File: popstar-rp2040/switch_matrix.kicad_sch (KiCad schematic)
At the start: 0 parts

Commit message: Added surface-mounted LEDs for shinethrough on WKL blockers.
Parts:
- added C18, C19, C20, C21, C22, C23, C24: 100nF, symbol Device:C_Small
- added D1, D10, D11, D12, D2, D3, D4, D5, D6, D7, D8, D9: WS2812_2020, marbastlib-various:LED_WS2812_2020, symbol marbastlib-various:WS2812_2020
- added U5: 74AHCT1G125, Package_TO_SOT_SMD:SOT-23-5, symbol 74xGxx:74AHCT1G125
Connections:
- new net: D2.1 (DOUT), D3.3 (DIN)
- new net: D1.1 (DOUT), D2.3 (DIN)
- new net: D5.1 (DOUT), D6.3 (DIN)
- new net: D4.1 (DOUT), D5.3 (DIN)
- new net: D11.1 (DOUT), D12.3 (DIN)
- new net: D10.1 (DOUT), D11.3 (DIN)
- new net: D3.1 (DOUT), D4.3 (DIN)
- new net: D6.1 (DOUT), D7.3 (DIN)
- new net: D10.3 (DIN), D9.1 (DOUT)
- new net: D8.1 (DOUT), D9.3 (DIN)
- new net: D7.1 (DOUT), D8.3 (DIN)
- new net +5V: C18.1, C19.1, C20.1, C21.1, C22.1, C23.1, C24.1, D1.4 (VDD), D10.4 (VDD), D11.4 (VDD), D12.4 (VDD), D2.4 (VDD), D3.4 (VDD), D4.4 (VDD), D5.4 (VDD), D6.4 (VDD), D7.4 (VDD), D8.4 (VDD), D9.4 (VDD), U5.5 (VCC)
- new net ARGB_3V3: U5.2
- new net ARGB_5V: D1.3 (DIN), U5.4
- new net GND: C18.2, C19.2, C20.2, C21.2, C22.2, C23.2, C24.2, D1.2 (VSS), D10.2 (VSS), D11.2 (VSS), D12.2 (VSS), D2.2 (VSS), D3.2 (VSS), D4.2 (VSS), D5.2 (VSS), D6.2 (VSS), D7.2 (VSS), D8.2 (VSS), D9.2 (VSS), U5.1, U5.3 (GND)
- no-connect marks 0 -> 1

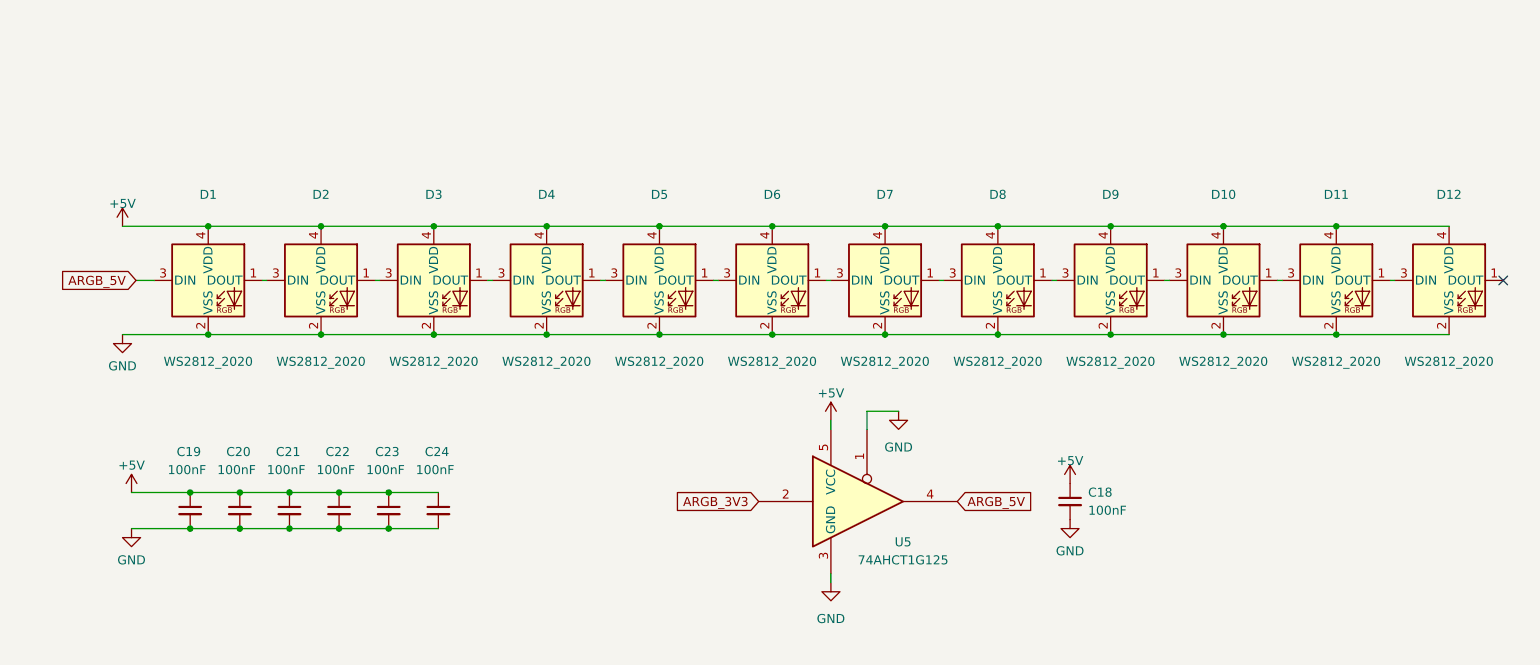
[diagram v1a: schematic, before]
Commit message: Cleaned up LED schematic impl.
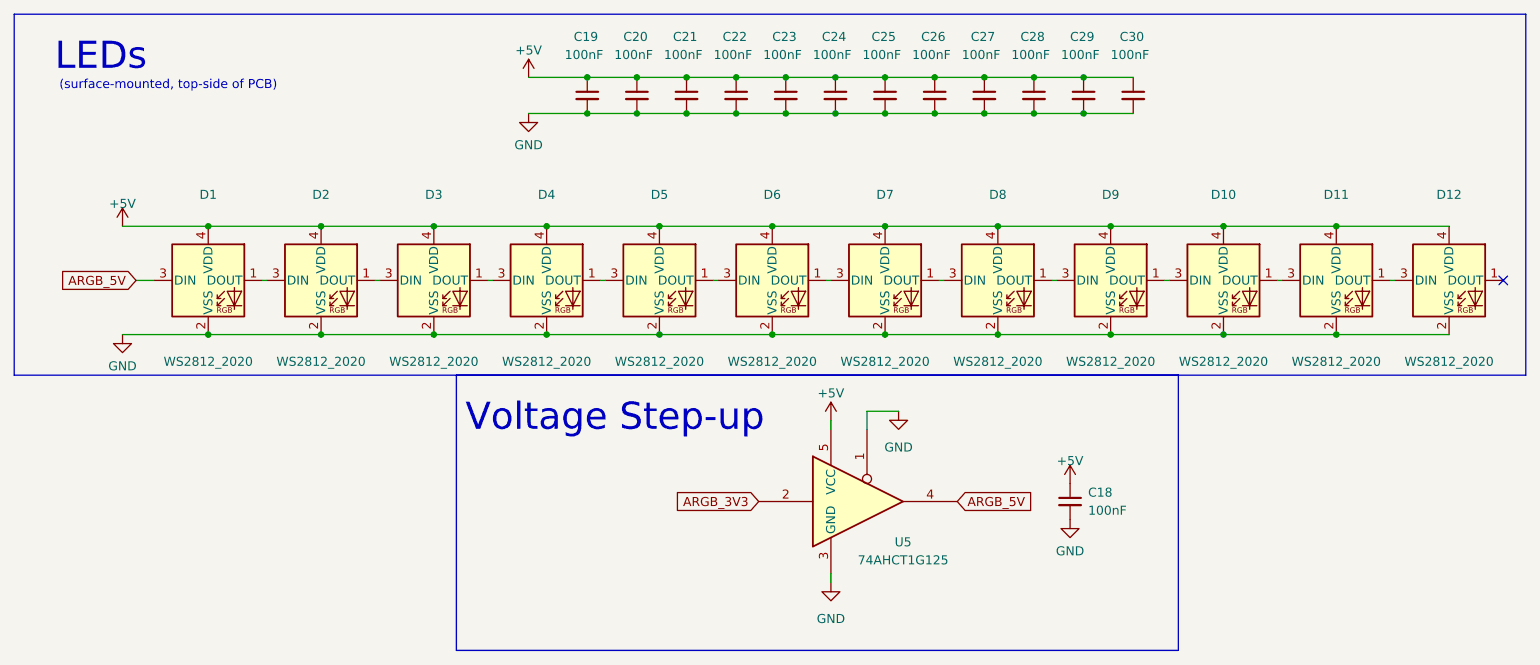
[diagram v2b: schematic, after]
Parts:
- added C25, C26, C27, C28, C29, C30: 100nF, symbol Device:C_Small
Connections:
- net +5V: now also C25.1, C26.1, C27.1, C28.1, C29.1, C30.1
- net GND: now also C25.2, C26.2, C27.2, C28.2, C29.2, C30.2
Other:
- note added: "(surface-mounted, top-side of PCB)"
- note added: "LEDs"
- note added: "Voltage Step-up"
- moved on the sheet: C19, C20, C21, C22, C23, C24

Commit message: Added BOM spreadsheet, updated components with LCSC part numbers and footprints.
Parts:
- C18, C19, C20, C21, C22, C23, C24, C25, C26, C27, C28, C29, C30: footprint (none) -> Capacitor_SMD:C_0402_1005Metric; LCSC (none) -> C1525
- U5: LCSC (none) -> C7484
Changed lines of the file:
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@@
       (effects (font (size 1.27 1.27)) (justify left))
     )
-    (property "Footprint" "" (at 170.18 119.38 0)
+    (property "Footprint" "Capacitor_SMD:C_0402_1005Metric" (at 170.18 119.38 0)
       (effects (font (size 1.27 1.27)) hide)
     )
@@
       (effects (font (size 1.27 1.27)) hide)
     )
+    (property "LCSC" "C1525" (at 170.18 119.38 0)
+      (effects (font (size 1.27 1.27)) hide)
+    )
     (pin "1")
     (pin "2")
@@
       (effects (font (size 1.27 1.27)) (justify left))
     )
-    (property "Footprint" "" (at 163.195 119.38 0)
+    (property "Footprint" "Capacitor_SMD:C_0402_1005Metric" (at 163.195 119.38 0)
       (effects (font (size 1.27 1.27)) hide)
     )
     (property "Datasheet" "~" (at 163.195 119.38 0)
+      (effects (font (size 1.27 1.27)) hide)
+    )
+    (property "LCSC" "C1525" (at 163.195 119.38 0)
       (effects (font (size 1.27 1.27)) hide)
     )
@@
       (effects (font (size 1.27 1.27)) (justify left))
     )
-    (property "Footprint" "" (at 93.345 119.38 0)
+    (property "Footprint" "Capacitor_SMD:C_0402_1005Metric" (at 93.345 119.38 0)
       (effects (font (size 1.27 1.27)) hide)
     )
@@
       (effects (font (size 1.27 1.27)) hide)
     )
+    (property "LCSC" "C1525" (at 93.345 119.38 0)
+      (effects (font (size 1.27 1.27)) hide)
+    )
     (pin "1")
     (pin "2")
@@
       (effects (font (size 1.27 1.27)) (justify left))
     )
-    (property "Footprint" "" (at 121.285 119.38 0)
+    (property "Footprint" "Capacitor_SMD:C_0402_1005Metric" (at 121.285 119.38 0)
       (effects (font (size 1.27 1.27)) hide)
     )
@@
       (effects (font (size 1.27 1.27)) hide)
     )
+    (property "LCSC" "C1525" (at 121.285 119.38 0)
+      (effects (font (size 1.27 1.27)) hide)
+    )
     (pin "1")
     (pin "2")
@@
       (effects (font (size 1.27 1.27)) (justify left))
     )
-    (property "Footprint" "" (at 128.27 119.38 0)
+    (property "Footprint" "Capacitor_SMD:C_0402_1005Metric" (at 128.27 119.38 0)
       (effects (font (size 1.27 1.27)) hide)
     )
@@
       (effects (font (size 1.27 1.27)) hide)
     )
+    (property "LCSC" "C1525" (at 128.27 119.38 0)
+      (effects (font (size 1.27 1.27)) hide)
+    )
     (pin "1")
     (pin "2")
@@
       (effects (font (size 1.27 1.27)) (justify left))
     )
-    (property "Footprint" "" (at 161.29 176.53 0)
+    (property "Footprint" "Capacitor_SMD:C_0402_1005Metric" (at 161.29 176.53 0)
       (effects (font (size 1.27 1.27)) hide)
     )
     (property "Datasheet" "~" (at 161.29 176.53 0)
+      (effects (font (size 1.27 1.27)) hide)
+    )
+    (property "LCSC" "C1525" (at 161.29 176.53 0)
       (effects (font (size 1.27 1.27)) hide)
     )
@@
       (effects (font (size 1.27 1.27)) (justify left))
     )
-    (property "Footprint" "" (at 142.24 119.38 0)
+    (property "Footprint" "Capacitor_SMD:C_0402_1005Metric" (at 142.24 119.38 0)
       (effects (font (size 1.27 1.27)) hide)
     )
@@
       (effects (font (size 1.27 1.27)) hide)
     )
+    (property "LCSC" "C1525" (at 142.24 119.38 0)
+      (effects (font (size 1.27 1.27)) hide)
+    )
     (pin "1")
     (pin "2")
@@
       (effects (font (size 1.27 1.27)) (justify left))
     )
-    (property "Footprint" "" (at 107.315 119.38 0)
+    (property "Footprint" "Capacitor_SMD:C_0402_1005Metric" (at 107.315 119.38 0)
       (effects (font (size 1.27 1.27)) hide)
     )
     (property "Datasheet" "~" (at 107.315 119.38 0)
+      (effects (font (size 1.27 1.27)) hide)
+    )
+    (property "LCSC" "C1525" (at 107.315 119.38 0)
       (effects (font (size 1.27 1.27)) hide)
     )
@@
       (effects (font (size 1.27 1.27)) (justify left))
     )
-    (property "Footprint" "" (at 100.33 119.38 0)
+    (property "Footprint" "Capacitor_SMD:C_0402_1005Metric" (at 100.33 119.38 0)
       (effects (font (size 1.27 1.27)) hide)
     )
@@
       (effects (font (size 1.27 1.27)) hide)
     )
+    (property "LCSC" "C1525" (at 100.33 119.38 0)
+      (effects (font (size 1.27 1.27)) hide)
+    )
     (pin "1")
     (pin "2")
@@
       (effects (font (size 1.27 1.27)) hide)
     )
+    (property "LCSC" "C7484" (at 132.715 176.53 0)
+      (effects (font (size 1.27 1.27)) hide)
+    )
     (pin "1")
     (pin "2")
@@
       (effects (font (size 1.27 1.27)) (justify left))
     )
-    (property "Footprint" "" (at 156.21 119.38 0)
+    (property "Footprint" "Capacitor_SMD:C_0402_1005Metric" (at 156.21 119.38 0)
       (effects (font (size 1.27 1.27)) hide)
     )
     (property "Datasheet" "~" (at 156.21 119.38 0)
+      (effects (font (size 1.27 1.27)) hide)
+    )
+    (property "LCSC" "C1525" (at 156.21 119.38 0)
       (effects (font (size 1.27 1.27)) hide)
     )
@@
       (effects (font (size 1.27 1.27)) (justify left))
     )
-    (property "Footprint" "" (at 114.3 119.38 0)
+    (property "Footprint" "Capacitor_SMD:C_0402_1005Metric" (at 114.3 119.38 0)
       (effects (font (size 1.27 1.27)) hide)
     )
@@
       (effects (font (size 1.27 1.27)) hide)
     )
+    (property "LCSC" "C1525" (at 114.3 119.38 0)
+      (effects (font (size 1.27 1.27)) hide)
+    )
     (pin "1")
     (pin "2")
@@
       (effects (font (size 1.27 1.27)) (justify left))
     )
-    (property "Footprint" "" (at 149.225 119.38 0)
+    (property "Footprint" "Capacitor_SMD:C_0402_1005Metric" (at 149.225 119.38 0)
       (effects (font (size 1.27 1.27)) hide)
     )
@@
       (effects (font (size 1.27 1.27)) hide)
     )
+    (property "LCSC" "C1525" (at 149.225 119.38 0)
+      (effects (font (size 1.27 1.27)) hide)
+    )
     (pin "1")
     (pin "2")
@@
       (effects (font (size 1.27 1.27)) (justify left))
     )
-    (property "Footprint" "" (at 135.255 119.38 0)
+    (property "Footprint" "Capacitor_SMD:C_0402_1005Metric" (at 135.255 119.38 0)
       (effects (font (size 1.27 1.27)) hide)
     )
@@
       (effects (font (size 1.27 1.27)) hide)
     )
+    (property "LCSC" "C1525" (at 135.255 119.38 0)
+      (effects (font (size 1.27 1.27)) hide)
+    )

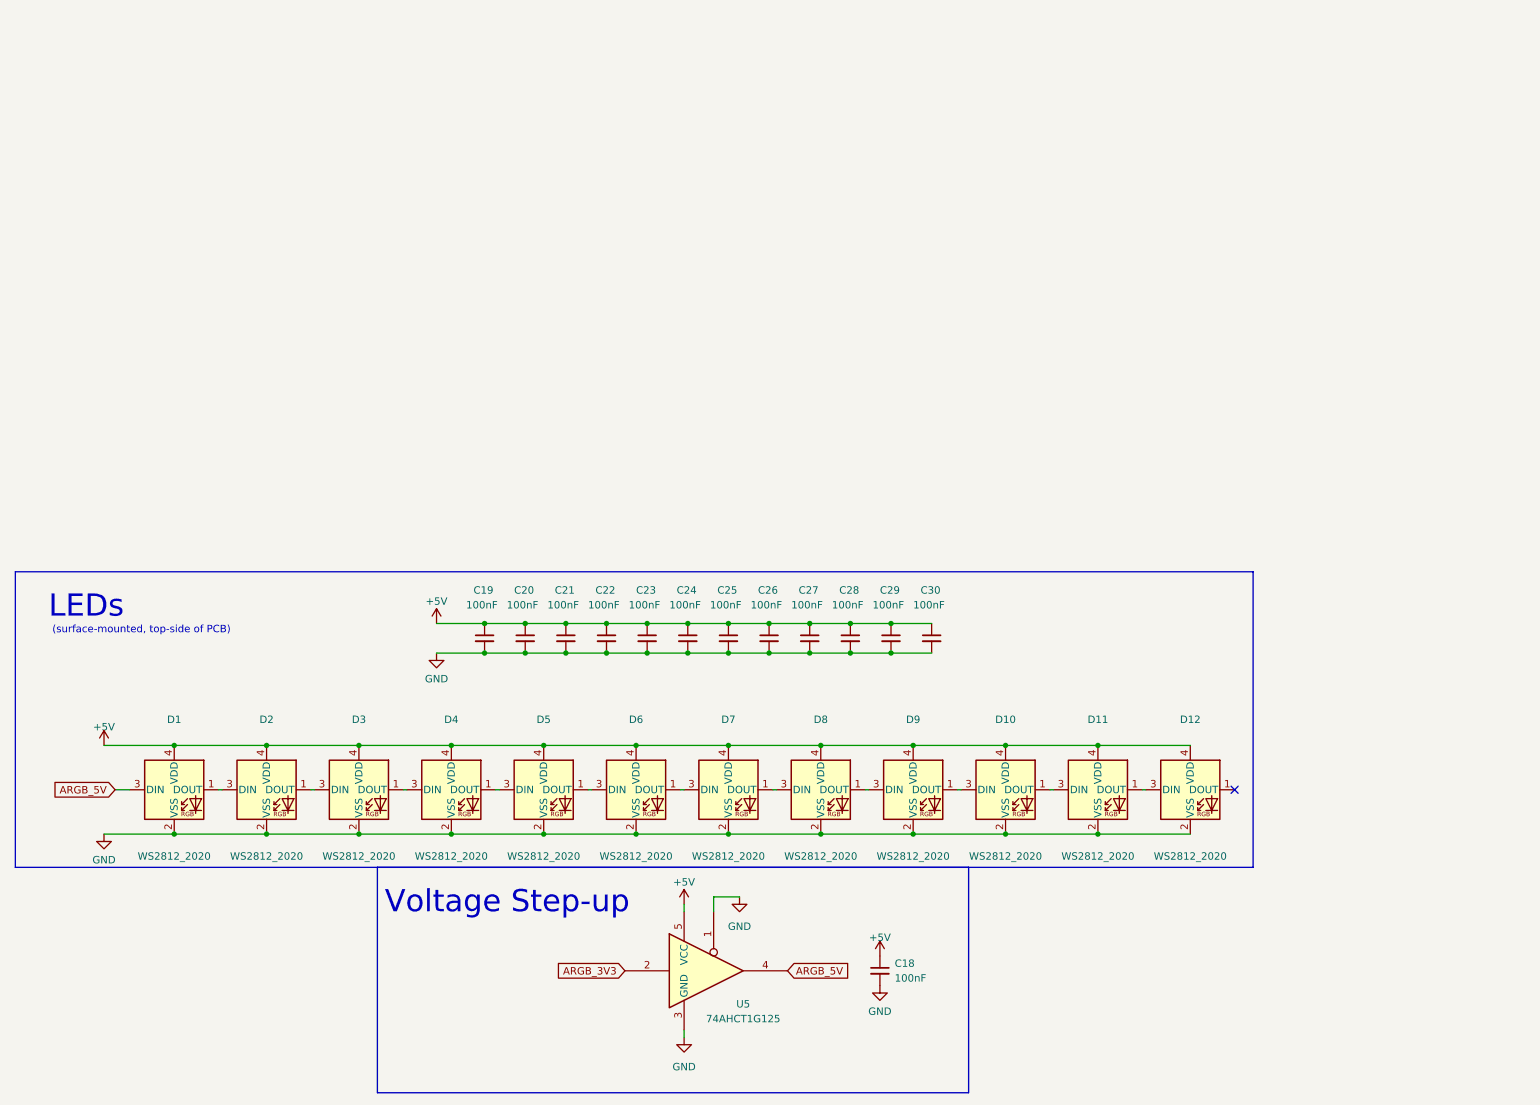
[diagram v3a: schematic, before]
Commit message: Finished switch matrix, updated pin connections accordingly
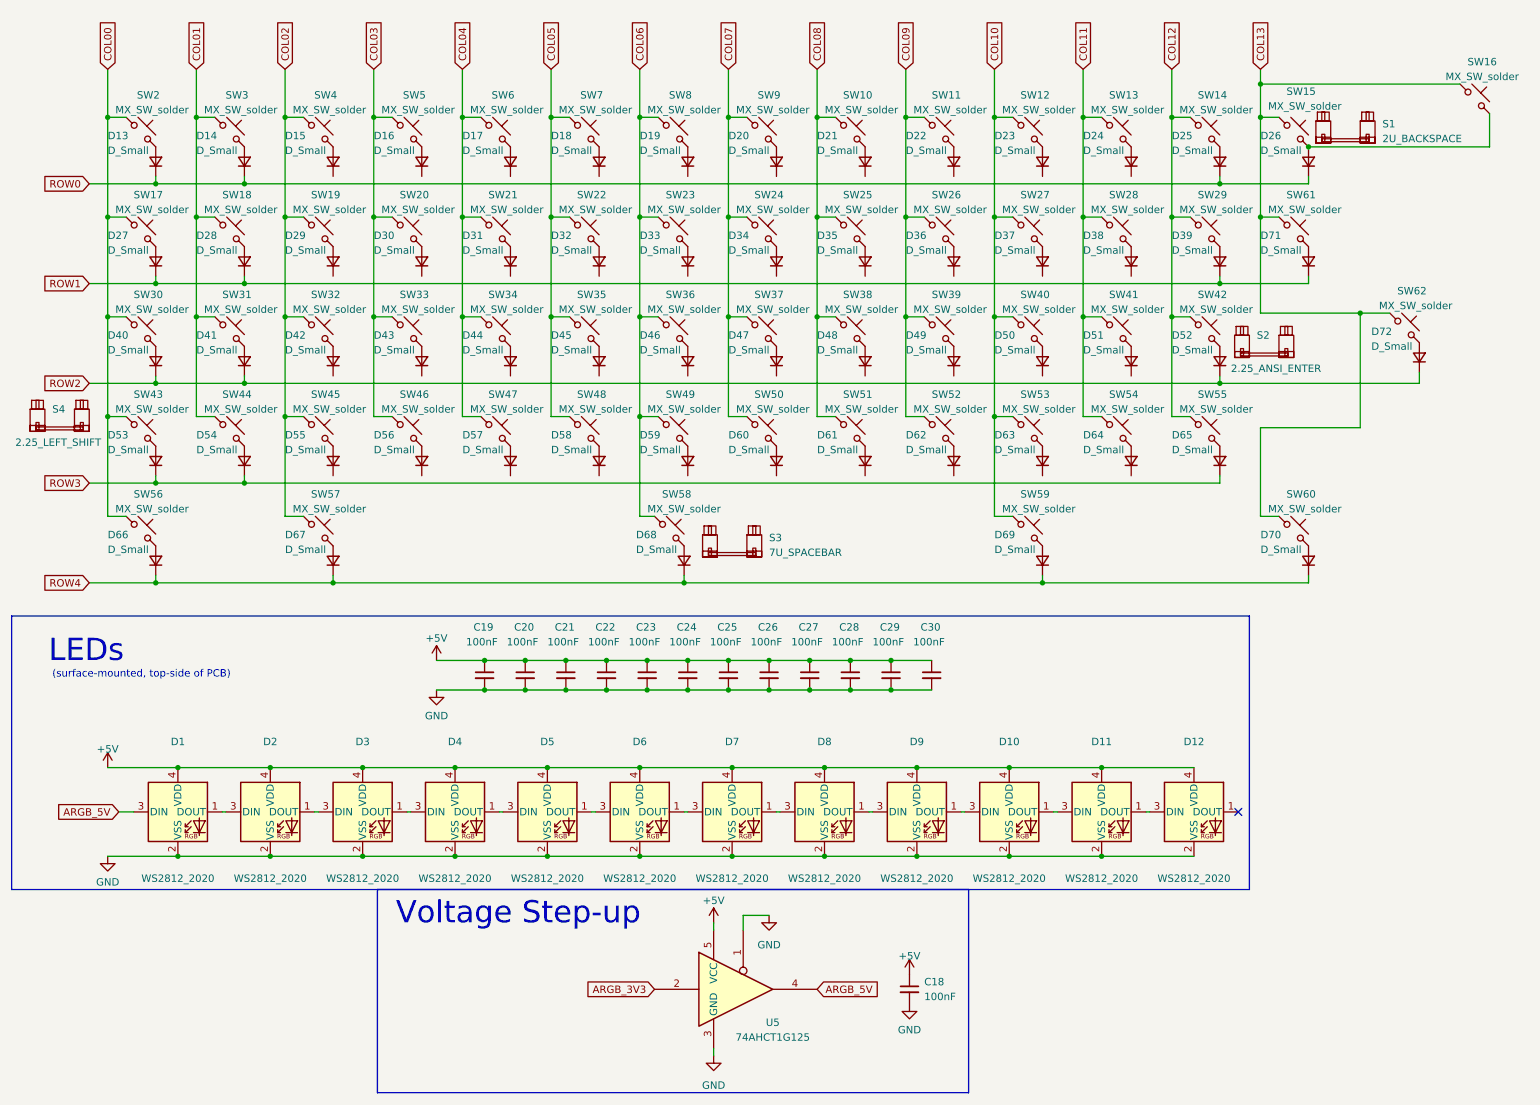
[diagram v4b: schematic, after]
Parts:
- added D13, D14, D15, D16, D17, D18, D19, D20, D21, D22, D23, D24, D25, D26, D27, D28, D29, D30, D31, D32, D33, D34, D35, D36, D37, D38, D39, D40, D41, D42, D43, D44, D45, D46, D47, D48, D49, D50, D51, D52, D53, D54, D55, D56, D57, D58, D59, D60, D61, D62, D63, D64, D65, D66, D67, D68, D69, D70, D71, D72: D_Small, Diode_SMD:D_SOD-123, symbol Device:D_Small
- added S1: 2U_BACKSPACE, marbastlib-mx:STAB_MX_2u, symbol marbastlib-mx:MX_stab
- added S2: 2.25_ANSI_ENTER, marbastlib-mx:STAB_MX_2.25u, symbol marbastlib-mx:MX_stab
- added S3: 7U_SPACEBAR, marbastlib-mx:STAB_MX_P_7u, symbol marbastlib-mx:MX_stab
- added S4: 2.25_LEFT_SHIFT, marbastlib-mx:STAB_MX_P_6.25u, symbol marbastlib-mx:MX_stab
- added SW10, SW11, SW12, SW13, SW14, SW15, SW16, SW18, SW19, SW2, SW20, SW21, SW22, SW23, SW24, SW25, SW26, SW27, SW28, SW29, SW3, SW31, SW32, SW33, SW34, SW35, SW36, SW37, SW38, SW39, SW4, SW40, SW41, SW42, SW43, SW44, SW45, SW46, SW47, SW48, SW49, SW5, SW50, SW51, SW52, SW53, SW55, SW58, SW6, SW61, SW7, SW8, SW9: MX_SW_solder, marbastlib-mx:SW_MX_1u, symbol marbastlib-mx:MX_SW_solder
- added SW17, SW56, SW57, SW59, SW60, SW62: MX_SW_solder, marbastlib-mx:SW_MX_1.5u, symbol marbastlib-mx:MX_SW_solder
- added SW30: MX_SW_solder, marbastlib-mx:SW_MX_1.75u_stp, symbol marbastlib-mx:MX_SW_solder
- added SW54: MX_SW_solder, marbastlib-mx:SW_MX_1.75u, symbol marbastlib-mx:MX_SW_solder
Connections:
- new net: D37.2 (A), SW27.2
- new net: D35.2 (A), SW25.2
- new net: D68.2 (A), SW58.2
- new net: D44.2 (A), SW34.2
- new net: D53.2 (A), SW43.2
- new net: D26.2 (A), SW15.2, SW16.2
- new net: D67.2 (A), SW57.2
- new net: D38.2 (A), SW28.2
- new net: D48.2 (A), SW38.2
- new net: D65.2 (A), SW55.2
- new net: D63.2 (A), SW53.2
- new net: D32.2 (A), SW22.2
- new net: D58.2 (A), SW48.2
- new net: D16.2 (A), SW5.2
- new net: D15.2 (A), SW4.2
- new net: D33.2 (A), SW23.2
- new net: D24.2 (A), SW13.2
- new net: D30.2 (A), SW20.2
- new net: D22.2 (A), SW11.2
- new net: D70.2 (A), SW60.2
- new net: D62.2 (A), SW52.2
- new net: D20.2 (A), SW9.2
- new net: D59.2 (A), SW49.2
- new net: D69.2 (A), SW59.2
- new net: D43.2 (A), SW33.2
- new net: D47.2 (A), SW37.2
- new net: D60.2 (A), SW50.2
- new net: D56.2 (A), SW46.2
- new net: D71.2 (A), SW61.2
- new net: D51.2 (A), SW41.2
- new net: D41.2 (A), SW31.2
- new net: D28.2 (A), SW18.2
- new net: D50.2 (A), SW40.2
- new net: D19.2 (A), SW8.2
- new net: D23.2 (A), SW12.2
- new net: D42.2 (A), SW32.2
- new net: D49.2 (A), SW39.2
- new net: D52.2 (A), SW42.2
- new net: D36.2 (A), SW26.2
- new net: D54.2 (A), SW44.2
- new net: D64.2 (A), SW54.2
- new net: D57.2 (A), SW47.2
- new net: D45.2 (A), SW35.2
- new net: D39.2 (A), SW29.2
- new net: D27.2 (A), SW17.2
- new net: D25.2 (A), SW14.2
- new net: D34.2 (A), SW24.2
- new net: D14.2 (A), SW3.2
- new net: D61.2 (A), SW51.2
- new net: D31.2 (A), SW21.2
- new net: D46.2 (A), SW36.2
- new net: D55.2 (A), SW45.2
- new net: D66.2 (A), SW56.2
- new net: D40.2 (A), SW30.2
- new net: D72.2 (A), SW62.2
- new net: D21.2 (A), SW10.2
- new net: D17.2 (A), SW6.2
- new net: D29.2 (A), SW19.2
- new net: D18.2 (A), SW7.2
- new net: D13.2 (A), SW2.2
- new net COL00: SW17.1, SW2.1, SW30.1, SW43.1, SW56.1
- new net COL01: SW18.1, SW3.1, SW31.1, SW44.1
- new net COL02: SW19.1, SW32.1, SW4.1, SW45.1, SW57.1
- new net COL03: SW20.1, SW33.1, SW46.1, SW5.1
- new net COL04: SW21.1, SW34.1, SW47.1, SW6.1
- new net COL05: SW22.1, SW35.1, SW48.1, SW7.1
- new net COL06: SW23.1, SW36.1, SW49.1, SW58.1, SW8.1
- new net COL07: SW24.1, SW37.1, SW50.1, SW9.1
- new net COL08: SW10.1, SW25.1, SW38.1, SW51.1
- new net COL09: SW11.1, SW26.1, SW39.1, SW52.1
- new net COL10: SW12.1, SW27.1, SW40.1, SW53.1, SW59.1
- new net COL11: SW13.1, SW28.1, SW41.1, SW54.1
- new net COL12: SW14.1, SW29.1, SW42.1, SW55.1
- new net COL13: SW15.1, SW16.1, SW60.1, SW61.1, SW62.1
- new net ROW0: D13.1 (K), D14.1 (K), D25.1 (K), D26.1 (K)
- new net ROW1: D27.1 (K), D28.1 (K), D39.1 (K), D71.1 (K)
- new net ROW2: D40.1 (K), D41.1 (K), D52.1 (K), D72.1 (K)
- new net ROW3: D53.1 (K), D54.1 (K), D65.1 (K)
- new net ROW4: D66.1 (K), D67.1 (K), D68.1 (K), D69.1 (K), D70.1 (K)
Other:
- moved on the sheet: C18, C19, C20, C21, C22, C23, C24, C25, C26, C27, C28, C29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
